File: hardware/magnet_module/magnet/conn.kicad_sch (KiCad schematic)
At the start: 11 parts, among them J1 Conn_01x03_Pin, J2 Conn_01x04_Pin, J3 Conn_01x04_Pin, J6 USB_C_Receptacle_USB2.0_14P, U1 ATA6561

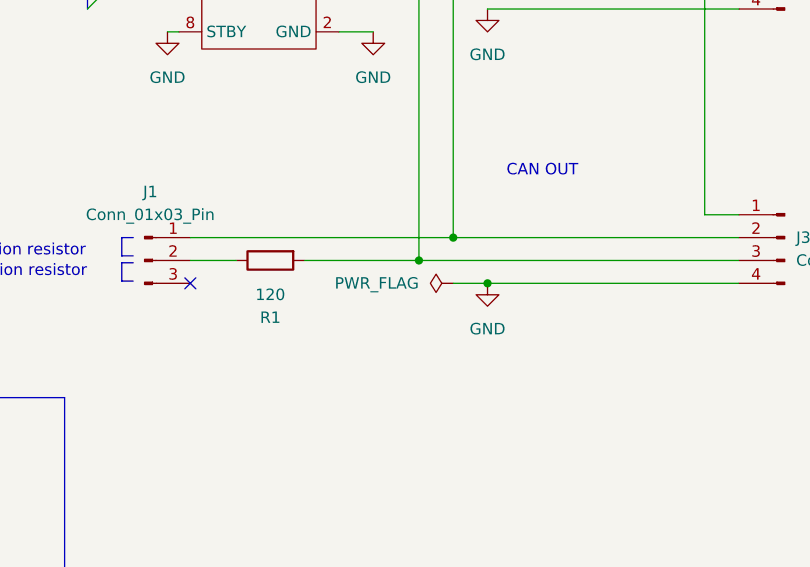
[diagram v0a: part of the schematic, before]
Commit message: fix erc errors
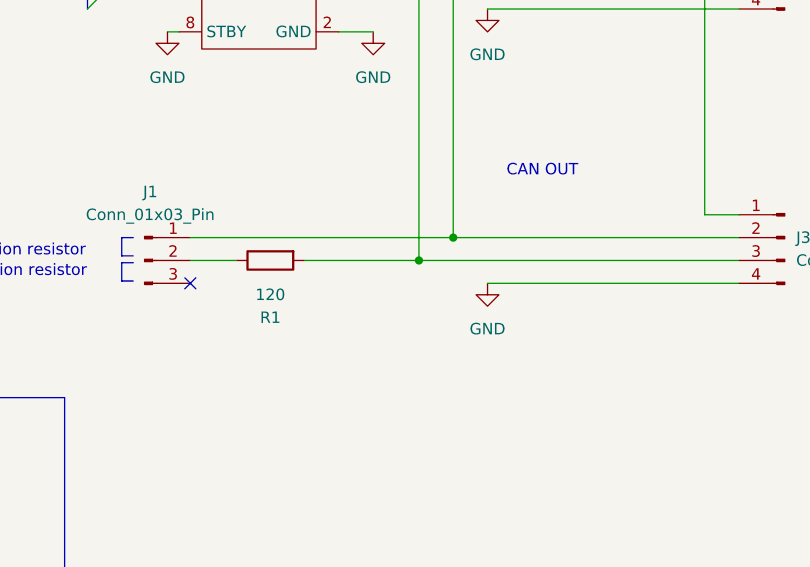
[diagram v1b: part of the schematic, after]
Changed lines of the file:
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@@
-	)
-	(junction
-		(at 158.75 118.11)
-		(diameter 0)
-		(color 0 0 0 0)
 	)
 	(junction
@@
 		(pts
 			(xy 97.79 78.74) (xy 97.79 81.28)
-		)
-		(stroke
-			(width 0)
-			(type default)
-		)
-	)
-	(wire
-		(pts
-			(xy 154.94 118.11) (xy 158.75 118.11)
 		)
 		(stroke
@@
 					(unit 1)
 				)
-			)
-		)
-	)
-	(symbol
-		(lib_id "power:PWR_FLAG")
-		(at 154.94 118.11 90)
-		(unit 1)
-		(exclude_from_sim no)
-		(in_bom yes)
-		(on_board yes)
-		(dnp no)
-		(fields_autoplaced yes)
-		(property "Reference" "#FLG01"
-			(at 153.035 118.11 0)
-			(effects
-				(font
-					(size 1.27 1.27)
-				)
-				(hide yes)
-			)
-		)
-		(property "Value" "PWR_FLAG"
-			(at 151.13 118.1099 90)
-			(effects
-				(font
-					(size 1.27 1.27)
-				)
-				(justify left)
-			)
-		)
-		(property "Footprint" ""
-			(at 154.94 118.11 0)
-			(effects
-				(font
-					(size 1.27 1.27)
-				)
-				(hide yes)
-			)
-		)
-		(property "Datasheet" "~"
-			(at 154.94 118.11 0)
-			(effects
-				(font
-					(size 1.27 1.27)
-				)
-				(hide yes)
-			)
-		)
-		(property "Description" "Special symbol for telling ERC where power comes from"
-			(at 154.94 118.11 0)
-			(effects
-				(font
-					(size 1.27 1.27)
-				)
-				(hide yes)
-			)
-		)
-		(pin "1"
-		)
-		(instances
-			(project "magnet"
-				(path "/aa5044b8-67cd-4b5a-a593-0df9431eb095/06f3621d-3ec0-4d63-9ba9-06465b135ad7"
-					(reference "#FLG01")
-					(unit 1)
-				)
